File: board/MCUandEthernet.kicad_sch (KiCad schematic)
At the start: 3 parts, among them J1 RJ45_LED_Shielded, U15 Teensy4.1_DEV-16771

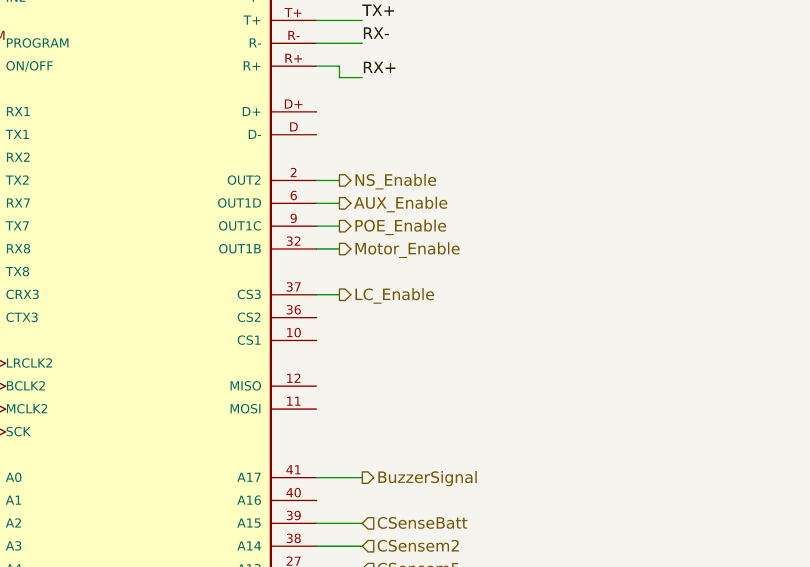
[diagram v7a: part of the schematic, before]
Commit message: include andersons for all LC and teensy enables for m2, m5, and m9
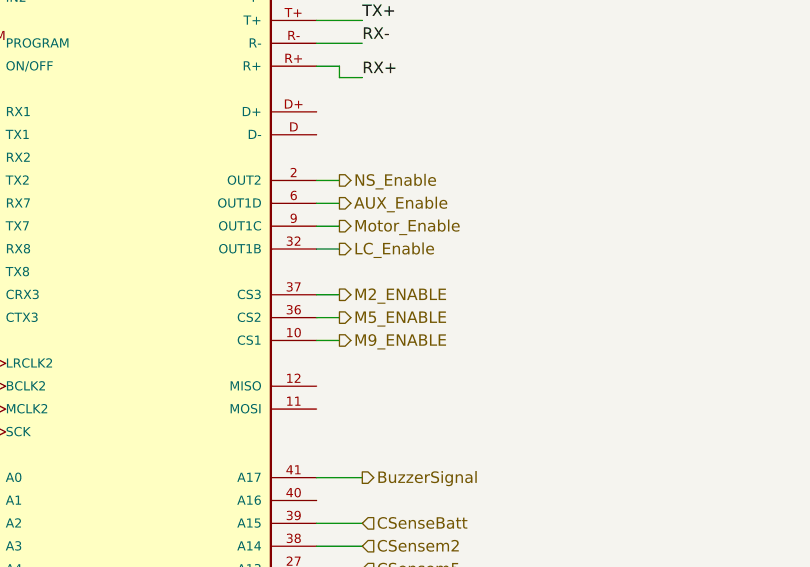
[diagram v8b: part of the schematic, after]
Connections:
- net POE_Enable is gone; now on net Motor_Enable: U15.9 (OUT1C)
- net LC_Enable: now also U15.32 (OUT1B); no longer U15.37 (CS3)
- net Motor_Enable: no longer U15.32 (OUT1B)
- net M9_ENABLE: now reaches U15.10 (CS1)
- net M5_ENABLE: now reaches U15.36 (CS2)
- new net M2_ENABLE: U15.37 (CS3)
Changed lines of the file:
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@@
+	(wire
+		(pts
+			(xy 68.58 99.06) (xy 71.12 99.06)
+		)
+		(stroke
+			(width 0)
+			(type default)
+		)
+	)
 	(wire
 		(pts
@@
 		(pts
 			(xy 26.67 83.82) (xy 27.94 83.82)
+		)
+		(stroke
+			(width 0)
+			(type default)
+		)
+	)
+	(wire
+		(pts
+			(xy 68.58 96.52) (xy 71.12 96.52)
 		)
 		(stroke
@@
 	(hierarchical_label "Motor_Enable"
 		(shape output)
+		(at 71.12 86.36 0)
+		(effects
+			(font
+				(size 1.27 1.27)
+			)
+			(justify left)
+		)
+	)
+	(hierarchical_label "CellSense2"
+		(shape input)
+		(at 24.13 116.84 180)
+		(effects
+			(font
+				(size 1.27 1.27)
+			)
+			(justify right)
+		)
+	)
+	(hierarchical_label "CellSense5"
+		(shape input)
+		(at 24.13 124.46 180)
+		(effects
+			(font
+				(size 1.27 1.27)
+			)
+			(justify right)
+		)
+	)
+	(hierarchical_label "CellSense6"
+		(shape input)
+		(at 24.13 127 180)
+		(effects
+			(font
+				(size 1.27 1.27)
+			)
+			(justify right)
+		)
+	)
+	(hierarchical_label "CSenseNS"
+		(shape input)
+		(at 73.66 132.08 0)
+		(effects
+			(font
+				(size 1.27 1.27)
+			)
+			(justify left)
+		)
+	)
+	(hierarchical_label "CellSense1"
+		(shape input)
+		(at 24.13 114.3 180)
+		(effects
+			(font
+				(size 1.27 1.27)
+			)
+			(justify right)
+		)
+	)
+	(hierarchical_label "M5_ENABLE"
+		(shape output)
+		(at 71.12 96.52 0)
+		(effects
+			(font
+				(size 1.27 1.27)
+			)
+			(justify left)
+		)
+	)
+	(hierarchical_label "E"
+		(shape output)
+		(at 25.4 101.6 180)
+		(effects
+			(font
+				(size 1.27 1.27)
+			)
+			(justify right)
+		)
+	)
+	(hierarchical_label "CSenseLC"
+		(shape input)
+		(at 73.66 129.54 0)
+		(effects
+			(font
+				(size 1.27 1.27)
+			)
+			(justify left)
+		)
+	)
+	(hierarchical_label "CSensem2"
+		(shape input)
+		(at 73.66 121.92 0)
+		(effects
+			(font
+				(size 1.27 1.27)
+			)
+			(justify left)
+		)
+	)
+	(hierarchical_label "RW"
+		(shape output)
+		(at 25.4 96.52 180)
+		(effects
+			(font
+				(size 1.27 1.27)
+			)
+			(justify right)
+		)
+	)
+	(hierarchical_label "CSenseAUX"
+		(shape input)
+		(at 73.66 134.62 0)
+		(effects
+			(font
+				(size 1.27 1.27)
+			)
+			(justify left)
+		)
+	)
+	(hierarchical_label "CSensem9"
+		(shape input)
+		(at 73.66 127 0)
+		(effects
+			(font
+				(size 1.27 1.27)
+			)
+			(justify left)
+		)
+	)
+	(hierarchical_label "AUX_Enable"
+		(shape output)
+		(at 71.12 83.82 0)
+		(effects
+			(font
+				(size 1.27 1.27)
+			)
+			(justify left)
+		)
+	)
+	(hierarchical_label "LC_Enable"
+		(shape output)
 		(at 71.12 88.9 0)
 		(effects
@@
 		)
 	)
-	(hierarchical_label "CellSense2"
-		(shape input)
-		(at 24.13 116.84 180)
+	(hierarchical_label "NS_Enable"
+		(shape output)
+		(at 71.12 81.28 0)
+		(effects
+			(font
+				(size 1.27 1.27)
+			)
+			(justify left)
+		)
+	)
+	(hierarchical_label "RS"
+		(shape output)
+		(at 25.4 93.98 180)
 		(effects
 			(font
@@
 		)
 	)
-	(hierarchical_label "CellSense5"
-		(shape input)
-		(at 24.13 124.46 180)
-		(effects
-			(font
-				(size 1.27 1.27)
-			)
-			(justify right)
-		)
-	)
-	(hierarchical_label "CellSense6"
-		(shape input)
-		(at 24.13 127 180)
-		(effects
-			(font
-				(size 1.27 1.27)
-			)
-			(justify right)
-		)
-	)
-	(hierarchical_label "CSenseNS"
-		(shape input)
-		(at 73.66 132.08 0)
-		(effects
-			(font
-				(size 1.27 1.27)
-			)
-			(justify left)
-		)
-	)
-	(hierarchical_label "CellSense1"
-		(shape input)
-		(at 24.13 114.3 180)
-		(effects
-			(font
-				(size 1.27 1.27)
-			)
-			(justify right)
-		)
-	)
-	(hierarchical_label "E"
-		(shape output)
-		(at 25.4 101.6 180)
-		(effects
-			(font
-				(size 1.27 1.27)
-			)
-			(justify right)
-		)
-	)
-	(hierarchical_label "CSenseLC"
-		(shape input)
-		(at 73.66 129.54 0)
-		(effects
-			(font
-				(size 1.27 1.27)
-			)
-			(justify left)
-		)
-	)
-	(hierarchical_label "CSensem2"
-		(shape input)
-		(at 73.66 121.92 0)
-		(effects
-			(font
-				(size 1.27 1.27)
-			)
-			(justify left)
-		)
-	)
-	(hierarchical_label "RW"
-		(shape output)
-		(at 25.4 96.52 180)
-		(effects
-			(font
-				(size 1.27 1.27)
-			)
-			(justify right)
-		)
-	)
-	(hierarchical_label "CSenseAUX"
-		(shape input)
-		(at 73.66 134.62 0)
-		(effects
-			(font
-				(size 1.27 1.27)
-			)
-			(justify left)
-		)
-	)
-	(hierarchical_label "CSensem9"
-		(shape input)
-		(at 73.66 127 0)
-		(effects
-			(font
-				(size 1.27 1.27)
-			)
-			(justify left)
-		)
-	)
-	(hierarchical_label "AUX_Enable"
-		(shape output)
-		(at 71.12 83.82 0)
-		(effects
-			(font
-				(size 1.27 1.27)
-			)
-			(justify left)
-		)
-	)
-	(hierarchical_label "LC_Enable"
-		(shape output)
-		(at 71.12 93.98 0)
-		(effects
-			(font
-				(size 1.27 1.27)
-			)
-			(justify left)
-		)
-	)
-	(hierarchical_label "NS_Enable"
-		(shape output)
-		(at 71.12 81.28 0)
-		(effects
-			(font
-				(size 1.27 1.27)
-			)
-			(justify left)
-		)
-	)
-	(hierarchical_label "RS"
-		(shape output)
-		(at 25.4 93.98 180)
-		(effects
-			(font
-				(size 1.27 1.27)
-			)
-			(justify right)
-		)
-	)
-	(hierarchical_label "POE_Enable"
-		(shape output)
-		(at 71.12 86.36 0)
-		(effects
-			(font
-				(size 1.27 1.27)
-			)
-			(justify left)
-		)
-	)
 	(hierarchical_label "CSenseBatt"
 		(shape input)
 		(at 73.66 119.38 0)
+		(effects
+			(font
+				(size 1.27 1.27)
+			)
+			(justify left)
+		)
+	)
+	(hierarchical_label "M9_ENABLE"
+		(shape output)
+		(at 71.12 99.06 0)
 		(effects
 			(font
@@
 		(effects
 			(font
+				(size 1.27 1.27)
+			)
+			(justify left)
+		)
+	)
+	(hierarchical_label "M2_ENABLE"
+		(shape output)
+		(at 71.12 93.98 0)
+		(effects
+			(font
